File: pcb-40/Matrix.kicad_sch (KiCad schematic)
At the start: 143 parts

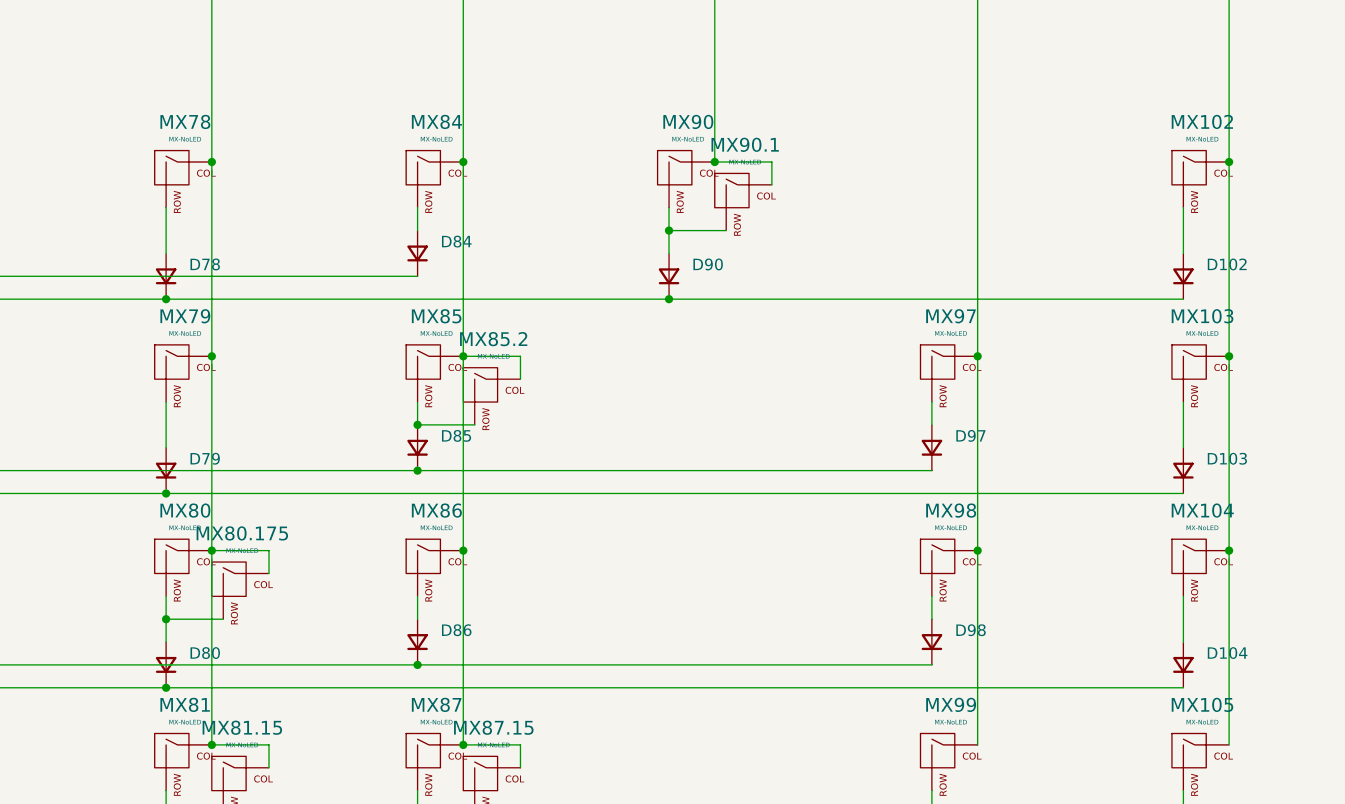
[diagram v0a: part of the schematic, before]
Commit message: Rev 2 improved layout
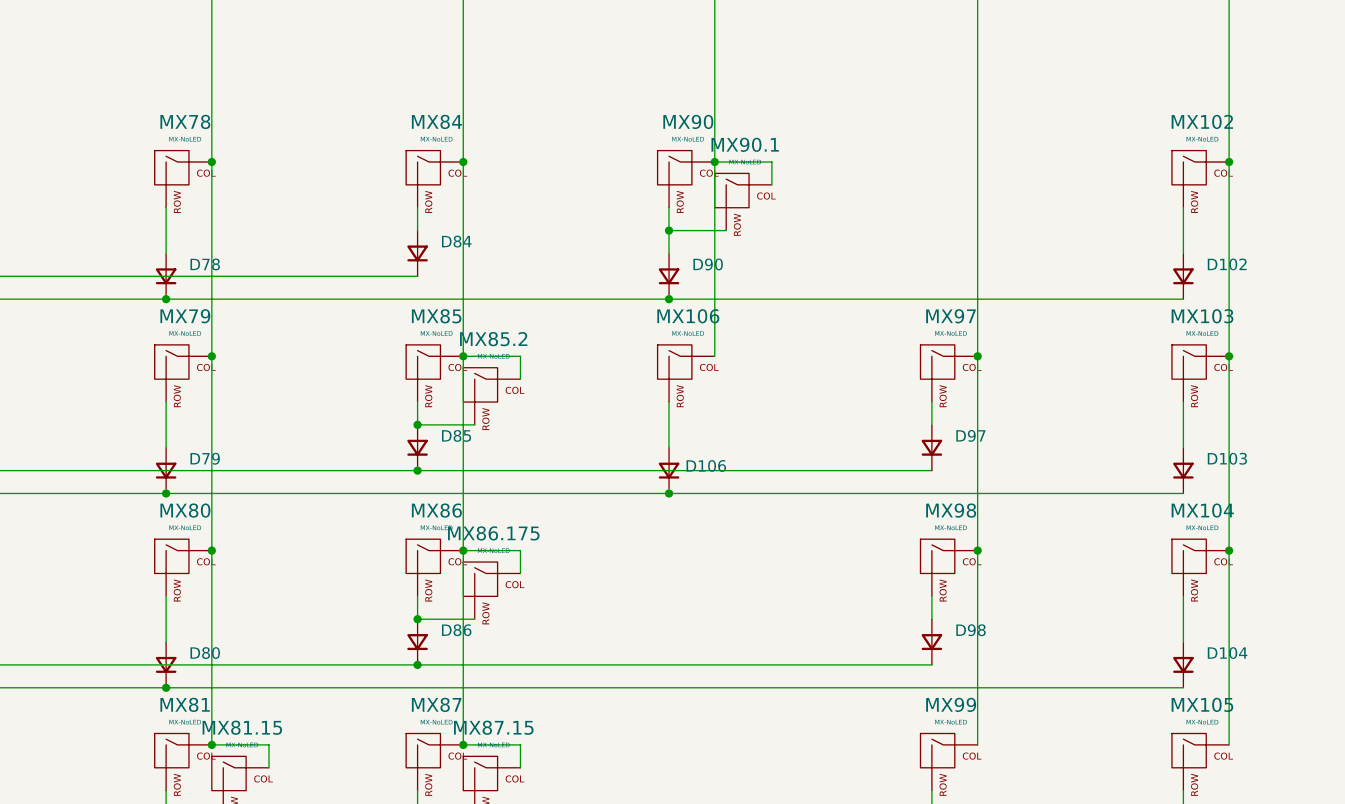
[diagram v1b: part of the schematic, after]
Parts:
- added D106: ~, symbol Device:D_Small
- added MX106: MX-NoLED, MX_Only:MXOnly-1U-NoLED, symbol MX_Alps_Hybrid:MX-NoLED
- renumbered MX80.175 to MX86.175
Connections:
- net COL5: no longer MX86.175.1 (COL)
- net COL6: now also MX86.175.1 (COL), MX106.1 (COL)
- net ROW9: now also D106.1 (K)
- net at D86.2 (A), MX86.2 (ROW): now also MX86.175.2 (ROW)
- net at D80.2 (A), MX80.2 (ROW): no longer MX86.175.2 (ROW)
- new net: D106.2 (A), MX106.2 (ROW)
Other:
- moved on the sheet: MX86.175
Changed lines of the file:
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@@
 	)
 	(junction
+		(at 420.37 153.67)
+		(diameter 0)
+		(color 0 0 0 0)
+	)
+	(junction
 		(at 420.37 180.34)
 		(diameter 0)
@@
 	)
 	(junction
+		(at 448.31 139.7)
+		(diameter 0)
+		(color 0 0 0 0)
+	)
+	(junction
 		(at 392.43 118.11)
 		(diameter 0)
@@
 	)
 	(junction
-		(at 392.43 153.67)
-		(diameter 0)
-		(color 0 0 0 0)
-	)
-	(junction
 		(at 510.54 59.69)
 		(diameter 0)
@@
 	(wire
 		(pts
+			(xy 448.31 139.7) (xy 505.46 139.7)
+		)
+		(stroke
+			(width 0)
+			(type default)
+		)
+	)
+	(wire
+		(pts
 			(xy 222.25 74.93) (xy 335.28 74.93)
 		)
@@
 	(wire
 		(pts
-			(xy 392.43 153.67) (xy 392.43 156.21)
+			(xy 392.43 151.13) (xy 392.43 156.21)
 		)
 		(stroke
@@
 	(wire
 		(pts
-			(xy 403.86 148.59) (xy 403.86 146.05)
+			(xy 431.8 148.59) (xy 431.8 146.05)
 		)
 		(stroke
@@
 	(wire
 		(pts
+			(xy 448.31 129.54) (xy 448.31 134.62)
+		)
+		(stroke
+			(width 0)
+			(type default)
+		)
+	)
+	(wire
+		(pts
 			(xy 453.39 48.26) (xy 453.39 59.69)
 		)
@@
 	(wire
 		(pts
+			(xy 453.39 102.87) (xy 453.39 124.46)
+		)
+		(stroke
+			(width 0)
+			(type default)
+		)
+	)
+	(wire
+		(pts
 			(xy 335.28 139.7) (xy 392.43 139.7)
 		)
@@
 	(wire
 		(pts
-			(xy 392.43 139.7) (xy 505.46 139.7)
+			(xy 392.43 139.7) (xy 448.31 139.7)
 		)
 		(stroke
@@
 	(wire
 		(pts
-			(xy 392.43 153.67) (xy 398.78 153.67)
+			(xy 420.37 153.67) (xy 426.72 153.67)
 		)
 		(stroke
@@
 	(wire
 		(pts
-			(xy 403.86 146.05) (xy 397.51 146.05)
+			(xy 431.8 146.05) (xy 425.45 146.05)
 		)
 		(stroke
@@
 	(wire
 		(pts
-			(xy 392.43 151.13) (xy 392.43 153.67)
-		)
-		(stroke
-			(width 0)
-			(type default)
-		)
-	)
-	(wire
-		(pts
 			(xy 392.43 175.26) (xy 392.43 177.8)
 		)
@@
 	(symbol
 		(lib_id "Device:D_Small")
+		(at 448.31 137.16 90)
+		(unit 1)
+		(exclude_from_sim no)
+		(in_bom yes)
+		(on_board yes)
+		(dnp no)
+		(fields_autoplaced yes)
+		(property "Reference" "D106"
+			(at 450.088 136.6908 90)
+			(effects
+				(font
+					(size 1.27 1.27)
+				)
+				(justify right)
+			)
+		)
+		(property "Value" "~"
+			(at 450.088 138.3722 90)
+			(effects
+				(font
+					(size 1.27 1.27)
+				)
+				(justify right)
+			)
+		)
+		(property "Footprint" ""
+			(at 448.31 137.16 90)
+			(effects
+				(font
+					(size 1.27 1.27)
+				)
+				(hide yes)
+			)
+		)
+		(property "Datasheet" "~"
+			(at 448.31 137.16 90)
+			(effects
+				(font
+					(size 1.27 1.27)
+				)
+				(hide yes)
+			)
+		)
+		(property "Description" ""
+			(at 448.31 137.16 0)
+			(effects
+				(font
+					(size 1.27 1.27)
+				)
+				(hide yes)
+			)
+		)
+		(property "LCSC" "C81598"
+			(at 448.31 137.16 0)
+			(effects
+				(font
+					(size 1.27 1.27)
+				)
+				(hide yes)
+			)
+		)
+		(pin "1"
+		)
+		(pin "2"
+		)
+		(instances
+			(project "pcb-40"
+				(path "/4811c7b7-222c-4bb6-b7b5-b7dd4d2eb234/02fdb854-e595-45dc-9fb2-56fe914219c3"
+					(reference "D106")
+					(unit 1)
+				)
+			)
+		)
+	)
+	(symbol
+		(lib_id "Device:D_Small")
 		(at 505.46 180.34 90)
 		(unit 1)
@@
 	(symbol
 		(lib_id "MX_Alps_Hybrid:MX-NoLED")
-		(at 400.05 149.86 0)
+		(at 427.99 149.86 0)
 		(unit 1)
 		(exclude_from_sim no)
@@
 		(on_board yes)
 		(dnp no)
-		(property "Reference" "MX80.175"
-			(at 400.8882 144.1958 0)
+		(property "Reference" "MX86.175"
+			(at 428.8282 144.1958 0)
 			(effects
 				(font
@@
 		)
 		(property "Value" "MX-NoLED"
-			(at 400.8882 146.0754 0)
+			(at 428.8282 146.0754 0)
 			(effects
 				(font
@@
 		)
 		(property "Footprint" "MX_Only:MXOnly-1U-NoLED"
-			(at 384.175 150.495 0)
+			(at 412.115 150.495 0)
 			(effects
 				(font
@@
 		)
 		(property "Datasheet" ""
-			(at 384.175 150.495 0)
+			(at 412.115 150.495 0)
 			(effects
 				(font
@@
 		)
 		(property "Description" ""
-			(at 400.05 149.86 0)
+			(at 427.99 149.86 0)
 			(effects
 				(font
@@
 			(project "pcb-40"
 				(path "/4811c7b7-222c-4bb6-b7b5-b7dd4d2eb234/02fdb854-e595-45dc-9fb2-56fe914219c3"
-					(reference "MX80.175")
+					(reference "MX86.175")
 					(unit 1)
 				)
@@
 					(unit 1)
 				)
+			)
+		)
+	)
+	(symbol
+		(lib_id "MX_Alps_Hybrid:MX-NoLED")
+		(at 449.58 125.73 0)
+		(unit 1)
+		(exclude_from_sim no)
+		(in_bom yes)
+		(on_board yes)
+		(dnp no)
+		(property "Reference" "MX106"
+			(at 450.4182 120.0658 0)
+			(effects
+				(font
+					(size 1.524 1.524)
+				)
+			)
+		)
+		(property "Value" "MX-NoLED"
+			(at 450.4182 121.9454 0)
+			(effects
+				(font
+					(size 0.508 0.508)
+				)
+			)
+		)
+		(property "Footprint" "MX_Only:MXOnly-1U-NoLED"
+			(at 433.705 126.365 0)
+			(effects
+				(font
+					(size 1.524 1.524)
+				)
+				(hide yes)
+			)
+		)
+		(property "Datasheet" ""
+			(at 433.705 126.365 0)
+			(effects
+				(font
+					(size 1.524 1.524)
+				)
+				(hide yes)
+			)
+		)
+		(property "Description" ""
+			(at 449.58 125.73 0)
+			(effects
+				(font
+					(size 1.27 1.27)
+				)
+				(hide yes)
+			)
+		)
+		(pin "1"
+		)
+		(pin "2"
+		)
+		(instances
+			(project "pcb-40"
+				(path "/4811c7b7-222c-4bb6-b7b5-b7dd4d2eb234/02fdb854-e595-45dc-9fb2-56fe914219c3"
+					(reference "MX106")
+					(unit 1)
+				)

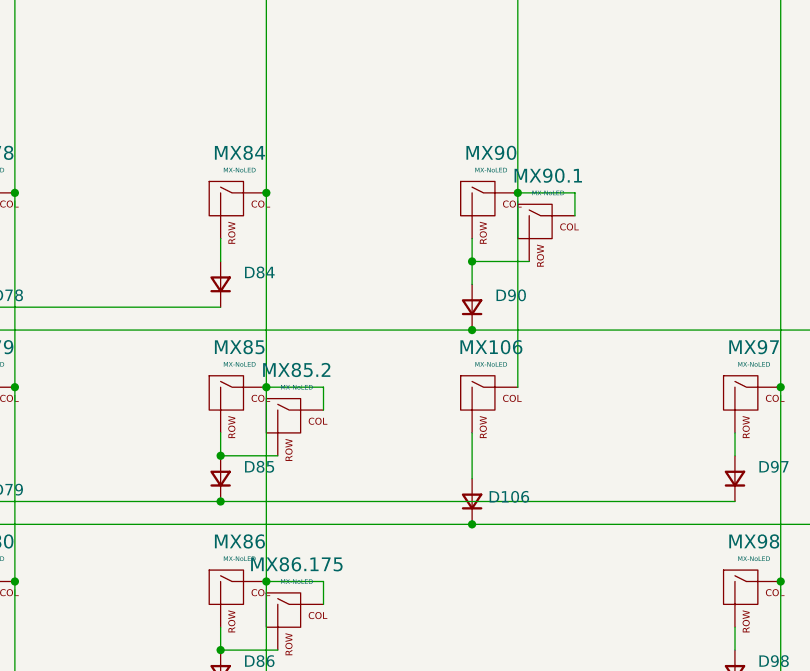
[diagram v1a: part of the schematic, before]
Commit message: Update readme and add firmware
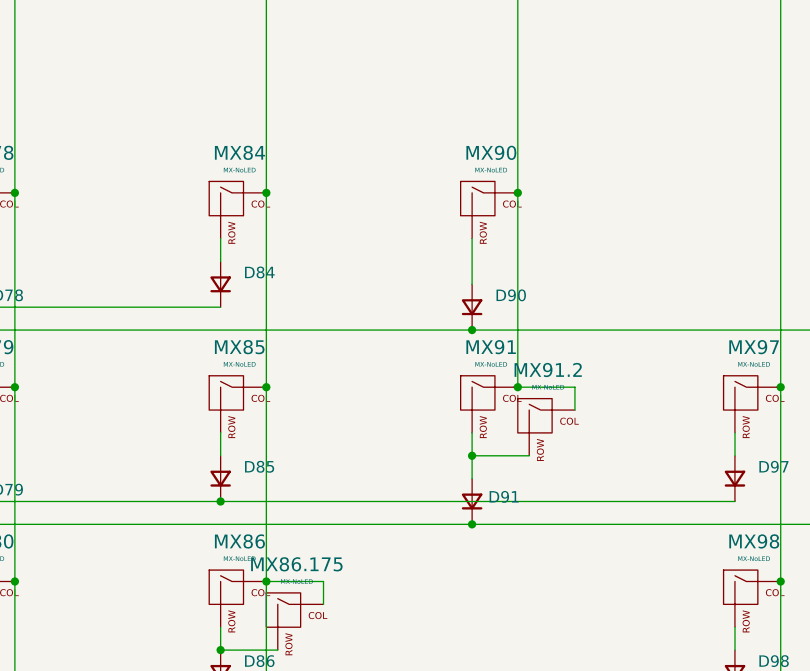
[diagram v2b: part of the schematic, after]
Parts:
- removed MX85.2: MX-NoLED, MX_Only:MXOnly-1U-NoLED, symbol MX_Alps_Hybrid:MX-NoLED
- renumbered D106 to D91, MX106 to MX91, MX90.1 to MX91.2
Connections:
- net at D91.2 (A), MX91.2 (ROW): now also MX91.2.2 (ROW)
- net at D90.2 (A), MX90.2 (ROW): no longer MX91.2.2 (ROW)
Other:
- moved on the sheet: MX91.2
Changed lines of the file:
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@@
 	)
 	(junction
-		(at 448.31 110.49)
+		(at 448.31 132.08)
 		(diameter 0)
 		(color 0 0 0 0)
@@
 	)
 	(junction
-		(at 420.37 132.08)
-		(diameter 0)
-		(color 0 0 0 0)
-	)
-	(junction
 		(at 166.37 139.7)
 		(diameter 0)
@@
 	)
 	(junction
+		(at 453.39 124.46)
+		(diameter 0)
+		(color 0 0 0 0)
+	)
+	(junction
 		(at 392.43 182.88)
 		(diameter 0)
@@
 	(wire
 		(pts
-			(xy 420.37 64.77) (xy 420.37 67.31)
+			(xy 448.31 132.08) (xy 448.31 134.62)
 		)
 		(stroke
@@
 	(wire
 		(pts
-			(xy 88.9 130.81) (xy 82.55 130.81)
+			(xy 420.37 64.77) (xy 420.37 67.31)
 		)
 		(stroke
@@
 	(wire
 		(pts
-			(xy 364.49 72.39) (xy 420.37 72.39)
+			(xy 88.9 130.81) (xy 82.55 130.81)
 		)
 		(stroke
@@
 	(wire
 		(pts
-			(xy 482.6 59.69) (xy 482.6 124.46)
+			(xy 364.49 72.39) (xy 420.37 72.39)
 		)
 		(stroke
@@
 	(wire
 		(pts
-			(xy 392.43 129.54) (xy 392.43 134.62)
+			(xy 482.6 59.69) (xy 482.6 124.46)
 		)
 		(stroke
@@
 	(wire
 		(pts
-			(xy 92.71 170.18) (xy 92.71 167.64)
+			(xy 392.43 129.54) (xy 392.43 134.62)
 		)
 		(stroke
@@
 	(wire
 		(pts
-			(xy 392.43 175.26) (xy 398.78 175.26)
+			(xy 92.71 170.18) (xy 92.71 167.64)
 		)
 		(stroke
@@
 	(wire
 		(pts
-			(xy 459.74 102.87) (xy 453.39 102.87)
+			(xy 392.43 175.26) (xy 398.78 175.26)
 		)
 		(stroke
@@
 	(wire
 		(pts
+			(xy 448.31 132.08) (xy 454.66 132.08)
+		)
+		(stroke
+			(width 0)
+			(type default)
+		)
+	)
+	(wire
+		(pts
 			(xy 448.31 74.93) (xy 505.46 74.93)
 		)
@@
 	(wire
 		(pts
-			(xy 448.31 129.54) (xy 448.31 134.62)
+			(xy 448.31 129.54) (xy 448.31 132.08)
 		)
 		(stroke
@@
 	(wire
 		(pts
-			(xy 138.43 172.72) (xy 138.43 175.26)
+			(xy 459.74 124.46) (xy 453.39 124.46)
 		)
 		(stroke
@@
 	(wire
 		(pts
-			(xy 482.6 124.46) (xy 482.6 146.05)
+			(xy 138.43 172.72) (xy 138.43 175.26)
 		)
 		(stroke
@@
 	(wire
 		(pts
-			(xy 205.74 167.64) (xy 199.39 167.64)
+			(xy 482.6 124.46) (xy 482.6 146.05)
 		)
 		(stroke
@@
 	(wire
 		(pts
-			(xy 227.33 102.87) (xy 227.33 124.46)
+			(xy 205.74 167.64) (xy 199.39 167.64)
 		)
 		(stroke
@@
 	(wire
 		(pts
-			(xy 194.31 137.16) (xy 307.34 137.16)
+			(xy 227.33 102.87) (xy 227.33 124.46)
 		)
 		(stroke
@@
 	(wire
 		(pts
-			(xy 431.8 127) (xy 431.8 124.46)
+			(xy 194.31 137.16) (xy 307.34 137.16)
 		)
 		(stroke
@@
 	(wire
 		(pts
-			(xy 448.31 107.95) (xy 448.31 110.49)
-		)
-		(stroke
-			(width 0)
-			(type default)
-		)
-	)
-	(wire
-		(pts
 			(xy 109.22 64.77) (xy 109.22 69.85)
 		)
@@
 	(wire
 		(pts
+			(xy 459.74 127) (xy 459.74 124.46)
+		)
+		(stroke
+			(width 0)
+			(type default)
+		)
+	)
+	(wire
+		(pts
 			(xy 76.2 180.34) (xy 81.28 180.34)
 		)
@@
 	(wire
 		(pts
-			(xy 448.31 110.49) (xy 448.31 113.03)
+			(xy 448.31 107.95) (xy 448.31 113.03)
 		)
 		(stroke
@@
 	(wire
 		(pts
-			(xy 448.31 110.49) (xy 454.66 110.49)
-		)
-		(stroke
-			(width 0)
-			(type default)
-		)
-	)
-	(wire
-		(pts
 			(xy 95.25 43.18) (xy 95.25 48.26)
 		)
@@
 	(wire
 		(pts
-			(xy 431.8 124.46) (xy 425.45 124.46)
-		)
-		(stroke
-			(width 0)
-			(type default)
-		)
-	)
-	(wire
-		(pts
 			(xy 199.39 48.26) (xy 199.39 59.69)
 		)
@@
 	(wire
 		(pts
-			(xy 420.37 132.08) (xy 426.72 132.08)
-		)
-		(stroke
-			(width 0)
-			(type default)
-		)
-	)
-	(wire
-		(pts
 			(xy 459.74 34.29) (xy 459.74 64.77)
 		)
@@
 	(wire
 		(pts
-			(xy 459.74 105.41) (xy 459.74 102.87)
-		)
-		(stroke
-			(width 0)
-			(type default)
-		)
-	)
-	(wire
-		(pts
 			(xy 222.25 161.29) (xy 335.28 161.29)
 		)
@@
 		(dnp no)
 		(fields_autoplaced yes)
-		(property "Reference" "D106"
+		(property "Reference" "D91"
 			(at 450.088 136.6908 90)
 			(effects
@@
 			(project "pcb-40"
 				(path "/4811c7b7-222c-4bb6-b7b5-b7dd4d2eb234/02fdb854-e595-45dc-9fb2-56fe914219c3"
-					(reference "D106")
+					(reference "D91")
 					(unit 1)
 				)
@@
 	(symbol
 		(lib_id "MX_Alps_Hybrid:MX-NoLED")
-		(at 455.93 106.68 0)
+		(at 455.93 128.27 0)
 		(unit 1)
 		(exclude_from_sim no)
@@
 		(on_board yes)
 		(dnp no)
-		(property "Reference" "MX90.1"
-			(at 456.7682 101.0158 0)
+		(property "Reference" "MX91.2"
+			(at 456.7682 122.6058 0)
 			(effects
 				(font
@@
 		)
 		(property "Value" "MX-NoLED"
-			(at 456.7682 102.8954 0)
+			(at 456.7682 124.4854 0)
 			(effects
 				(font
@@
 		)
 		(property "Footprint" "MX_Only:MXOnly-1U-NoLED"
-			(at 440.055 107.315 0)
+			(at 440.055 128.905 0)
 			(effects
 				(font
@@
 		)
 		(property "Datasheet" ""
-			(at 440.055 107.315 0)
+			(at 440.055 128.905 0)
 			(effects
 				(font
@@
 		)
 		(property "Description" ""
-			(at 455.93 106.68 0)
+			(at 455.93 128.27 0)
 			(effects
 				(font
@@
 			(project "pcb-40"
 				(path "/4811c7b7-222c-4bb6-b7b5-b7dd4d2eb234/02fdb854-e595-45dc-9fb2-56fe914219c3"
-					(reference "MX90.1")
+					(reference "MX91.2")
 					(unit 1)
 				)
@@
 	(symbol
 		(lib_id "MX_Alps_Hybrid:MX-NoLED")
-		(at 427.99 128.27 0)
-		(unit 1)
-		(exclude_from_sim no)
-		(in_bom yes)
-		(on_board yes)
-		(dnp no)
-		(property "Reference" "MX85.2"
-			(at 428.8282 122.6058 0)
-			(effects
-				(font
-					(size 1.524 1.524)
-				)
-			)
-		)
-		(property "Value" "MX-NoLED"
-			(at 428.8282 124.4854 0)
-			(effects
-				(font
-					(size 0.508 0.508)
-				)
-			)
-		)
-		(property "Footprint" "MX_Only:MXOnly-1U-NoLED"
-			(at 412.115 128.905 0)
-			(effects
-				(font
-					(size 1.524 1.524)
-				)
-				(hide yes)
-			)
-		)
-		(property "Datasheet" ""
-			(at 412.115 128.905 0)
-			(effects
-				(font
-					(size 1.524 1.524)
-				)
-				(hide yes)
-			)
-		)
-		(property "Description" ""
-			(at 427.99 128.27 0)
-			(effects
-				(font
-					(size 1.27 1.27)
-				)
-				(hide yes)
-			)
-		)
-		(pin "1"
-		)
-		(pin "2"
-		)
-		(instances
-			(project "pcb-40"
-				(path "/4811c7b7-222c-4bb6-b7b5-b7dd4d2eb234/02fdb854-e595-45dc-9fb2-56fe914219c3"
-					(reference "MX85.2")
-					(unit 1)
-				)
-			)
-		)
-	)
-	(symbol
-		(lib_id "MX_Alps_Hybrid:MX-NoLED")
 		(at 88.9 149.86 0)
 		(unit 1)
@@
 		(on_board yes)
 		(dnp no)
-		(property "Reference" "MX106"
+		(property "Reference" "MX91"
 			(at 450.4182 120.0658 0)
 			(effects
@@
 			(project "pcb-40"
 				(path "/4811c7b7-222c-4bb6-b7b5-b7dd4d2eb234/02fdb854-e595-45dc-9fb2-56fe914219c3"
-					(reference "MX106")
+					(reference "MX91")
 					(unit 1)
 				)
